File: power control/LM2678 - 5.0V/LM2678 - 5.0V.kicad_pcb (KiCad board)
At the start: 2 copper layers, 71.1 x 61.7 mm, 9 parts, among them J1 Conn_01x02_Pin, J3 Conn_01x03_Pin, U2 LM2678S-12

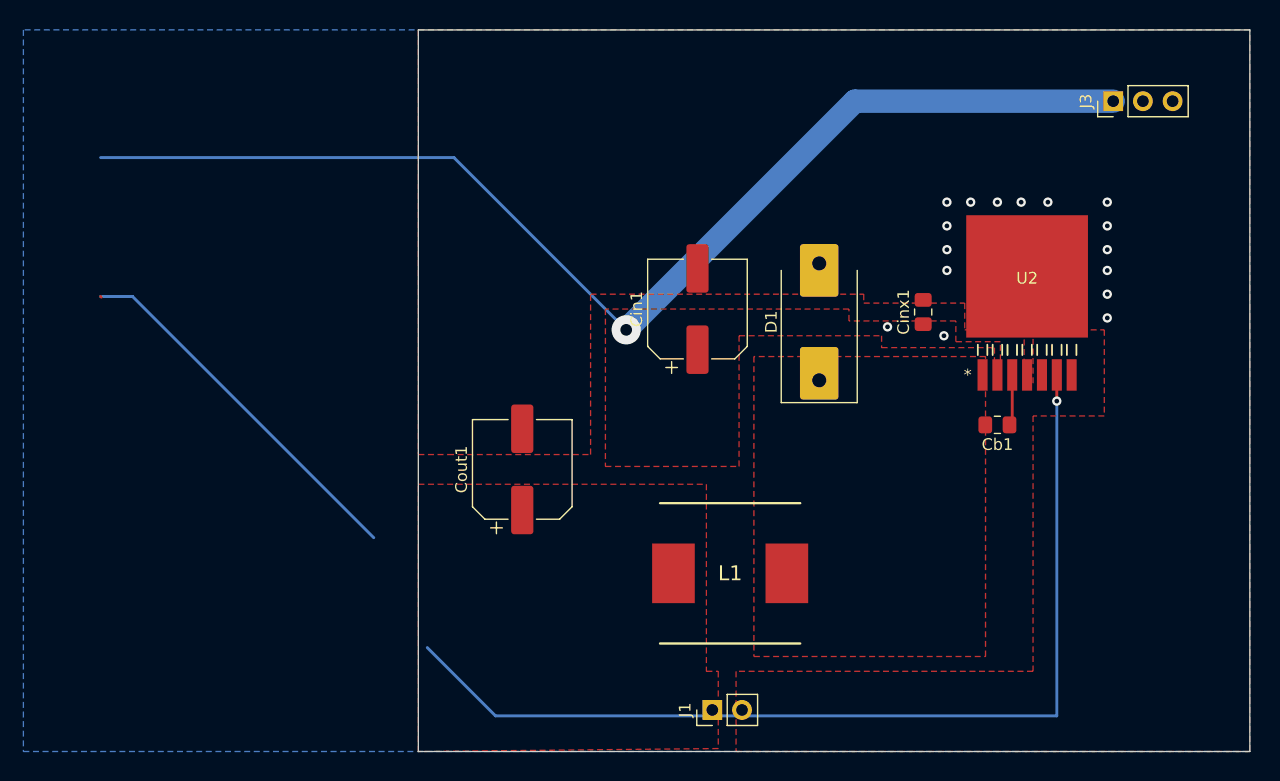
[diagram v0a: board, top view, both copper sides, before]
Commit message: modified power control to remove old regulator
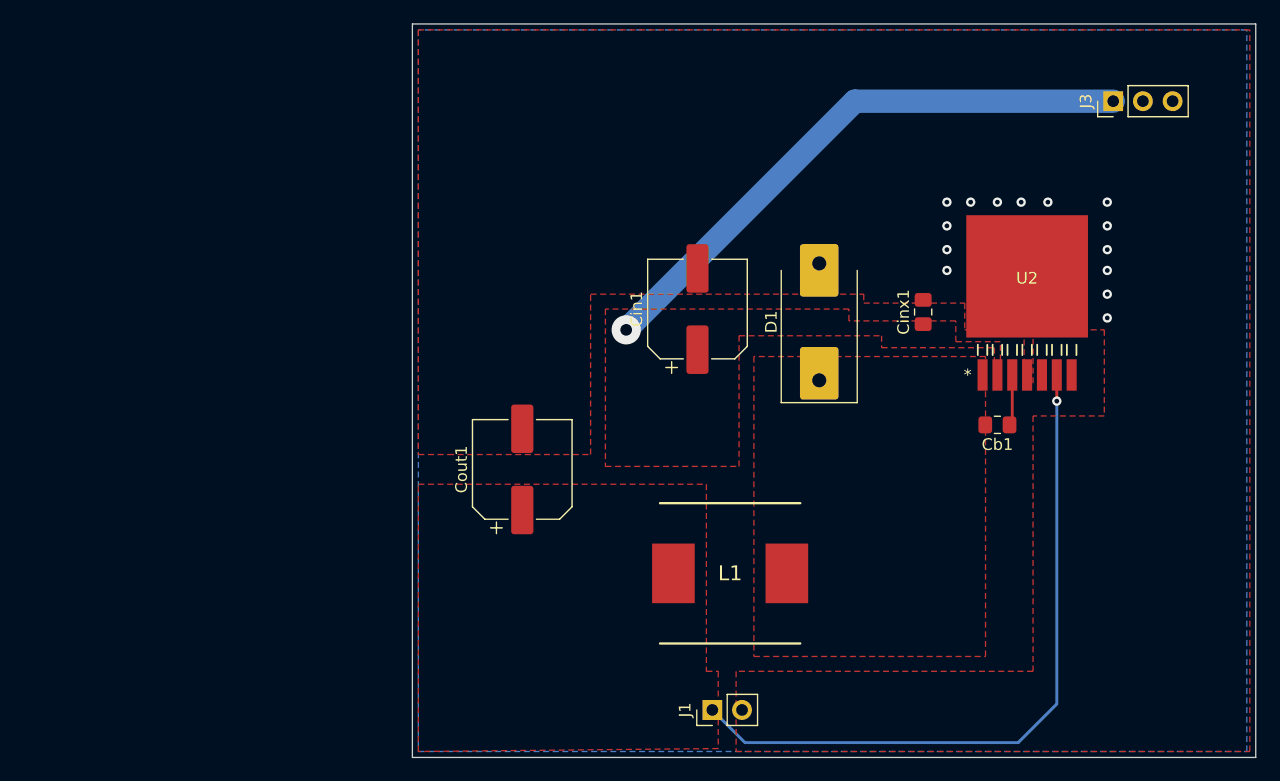
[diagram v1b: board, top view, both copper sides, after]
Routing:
- net /Vin: track 100.8 -> 49.8 mm, vias 3 -> 1
- net (no net): track 32.0 -> 0.00 mm
- net Net-(J1-Pin_1): track 85.4 -> 60.1 mm
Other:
- board size 71.1 x 61.7 mm -> 72.1 x 62.7 mm
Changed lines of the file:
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@@
     )
   )
-  (gr_rect (start 106.68 75.438) (end 177.8 137.16)
+  (gr_rect (start 106.172 74.93) (end 178.308 137.668)
     (stroke (width 0.1) (type default)) (fill none) (layer "Edge.Cuts"))
-  (segment (start 79.502 98.24) (end 79.56 98.298) (width 0.25) (layer "F.Cu") (net 0))
-  (segment (start 102.87 118.872) (end 82.238 98.24) (width 0.25) (layer "B.Cu") (net 0))
-  (segment (start 82.238 98.24) (end 79.502 98.24) (width 0.25) (layer "B.Cu") (net 0))
   (segment (start 157.734 95.504) (end 158.75 96.52) (width 0.25) (layer "F.Cu") (net 4))
   (via (at 160.528 90.17) (size 0.8) (drill 0.4) (layers "F.Cu" "B.Cu") (free) (net 4))
@@
   (segment (start 161.29 104.9528) (end 161.29 107.188) (width 0.25) (layer "F.Cu") (net 6))
   (via (at 161.29 107.188) (size 0.8) (drill 0.4) (layers "F.Cu" "B.Cu") (net 6))
-  (segment (start 161.29 107.188) (end 161.29 134.112) (width 0.25) (layer "B.Cu") (net 6))
-  (segment (start 161.29 134.112) (end 113.284 134.112) (width 0.25) (layer "B.Cu") (net 6))
-  (segment (start 113.284 134.112) (end 107.442 128.27) (width 0.25) (layer "B.Cu") (net 6))
+  (segment (start 157.988 136.398) (end 134.62 136.398) (width 0.25) (layer "B.Cu") (net 6))
+  (segment (start 161.29 133.096) (end 157.988 136.398) (width 0.25) (layer "B.Cu") (net 6))
+  (segment (start 161.29 107.188) (end 161.29 133.096) (width 0.25) (layer "B.Cu") (net 6))
+  (segment (start 134.62 136.398) (end 131.826 133.604) (width 0.25) (layer "B.Cu") (net 6))
   (via (at 124.46 101.092) (size 2.5) (drill 1) (layers "F.Cu" "B.Cu") (net 7))
-  (via (at 151.638 101.6) (size 0.8) (drill 0.4) (layers "F.Cu" "B.Cu") (net 7))
-  (via (at 146.812 100.838) (size 0.8) (drill 0.4) (layers "F.Cu" "B.Cu") (net 7))
-  (segment (start 109.728 86.36) (end 79.502 86.36) (width 0.25) (layer "B.Cu") (net 7))
   (segment (start 166.116 81.534) (end 144.018 81.534) (width 2) (layer "B.Cu") (net 7))
   (segment (start 144.018 81.534) (end 124.46 101.092) (width 2) (layer "B.Cu") (net 7))
-  (segment (start 124.46 101.092) (end 109.728 86.36) (width 0.25) (layer "B.Cu") (net 7))
   (zone (net 7) (net_name "/Vin") (layer "F.Cu") (hatch edge 0.5)
     (priority 3)
@@
     (polygon
       (pts
-        (xy 72.898 75.438)
-        (xy 72.898 137.16)
-        (xy 177.8 137.16)
-        (xy 177.8 75.438)
+        (xy 106.68 75.438)
+        (xy 106.68 137.16)
+        (xy 177.546 137.16)
+        (xy 177.546 75.438)
       )
     )
